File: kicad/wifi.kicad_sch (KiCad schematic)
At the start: 23 parts, among them J601 Conn_Coaxial, U302 NRF7002-QFAA-Rx, Y601 40MHz

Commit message: new board
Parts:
- added U603: TCK106AF, mylib_ic:SOT-25, symbol mylib_ic:TCK106AF
- C601: Digikey 1276-1040-2-ND -> 1276-1040-1-ND
- C602, C617: Digikey 478-7888-2-ND -> 478-7888-1-ND
- C603, C607, C615: Digikey 445-9090-2-ND -> 445-9090-1-ND
- C604, C605, C608, C616: Digikey 490-GRM155C61E475ME15DTR-ND -> 490-GRM155C61E475ME15DCT-ND
- C606, C611, C614: Digikey 1276-1067-2-ND -> 1276-1067-1-ND
- C609: Digikey 1276-1049-2-ND -> 1276-1049-1-ND
- C610, C618: Digikey 1276-1477-2-ND -> 1276-1477-1-ND
- C612: Digikey 1276-1028-2-ND -> 1276-1028-1-ND
- C613: Digikey 1276-1538-2-ND -> 1276-1538-1-ND
- J601: Digikey 343-CONMHF1-SMD-G-TTR-ND -> 343-CONMHF1-SMD-G-TCT-ND
- L601: Digikey 490-5115-2-ND -> 490-5115-1-ND
- U302: Digikey 4823-NRF7002-QFAA-R7TR-ND -> 4823-NRF7002-QFAA-R7CT-ND
- U602: symbol mylib_connectors:DPX1608 -> mylib_ic:DPX1608; Digikey 553-DPX1608LL80R2455ATR-ND -> 553-DPX1608LL80R2455ACT-ND
- Y601: Digikey 478-CX2016DB40000D0FLJCCTR-ND -> 478-CX2016DB40000D0FLJCCCT-ND
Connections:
- net +3V3: now also U603.5 (V_{IN}); no longer C601.1, U302.48 (IOVDD)
- net GND: now also U603.2 (GND)
- new net IOVDD: C601.1, U302.48 (IOVDD), U603.1 (V_{OUT})
- new net WIFI_ENABLE: U603.3 (CTRL)
- now unconnected: U302.2 (N.C.), U302.21 (N.C.), U302.22 (N.C.), U302.23 (N.C.), U302.24 (N.C.), U302.3 (N.C.), U302.4 (N.C.), U302.5 (N.C.), U302.6 (N.C.)

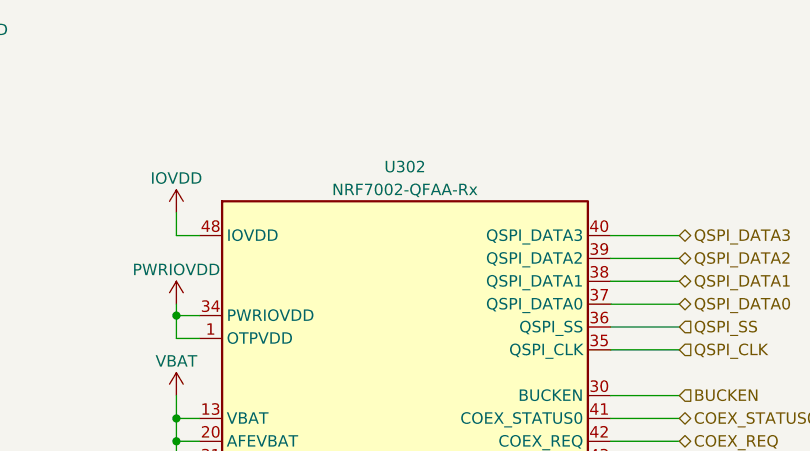
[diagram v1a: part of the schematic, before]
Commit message: upgrade 2 KiCAD 8.0
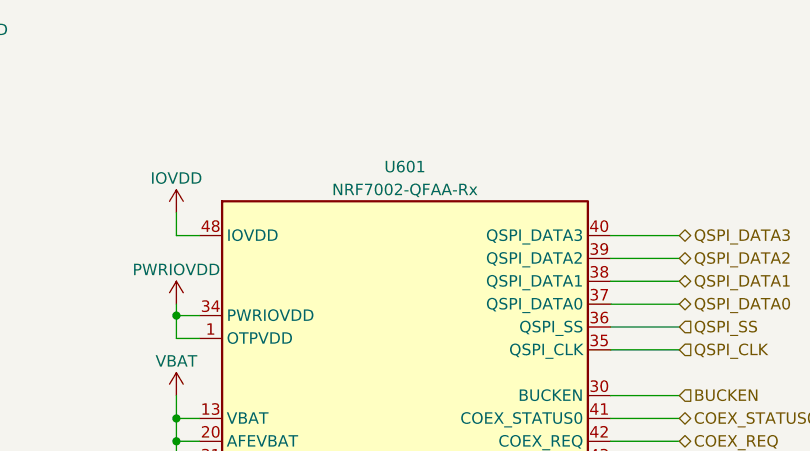
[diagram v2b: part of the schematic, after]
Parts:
- renumbered U302 to U601
